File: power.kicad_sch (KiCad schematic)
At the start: 37 parts, among them J1 +5V SUPPLY, SW1 RESET, U1 NS32201, U19 74AHC32, U2 LM3671, U3 NS32016, U4 NS32082, U5 NS32202, U6 74AHC08, Y1 12.00000MHz

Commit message: merge in rev4
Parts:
- C7: value 2.2µF -> 0.1µF; footprint Capacitor_SMD:C_0603_1608Metric -> Capacitor_SMD:C_0402_1005Metric
- R6: value 47k -> 1k
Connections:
- net ~{RESET}: now also C7.1, R6.2, SW1.1, U1.7 (~{RSTI}); no longer U3.34 (~{RST}/ABT), U4.34 (~{RST}/ABT), U5.27 (~{RST})
- new net: U3.34 (~{RST}/ABT), U4.34 (~{RST}/ABT), U5.27 (~{RST})
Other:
- moved on the sheet: C1, C10, C11, C12, C14, C15, C16, C18, C2, C20, C3, C4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

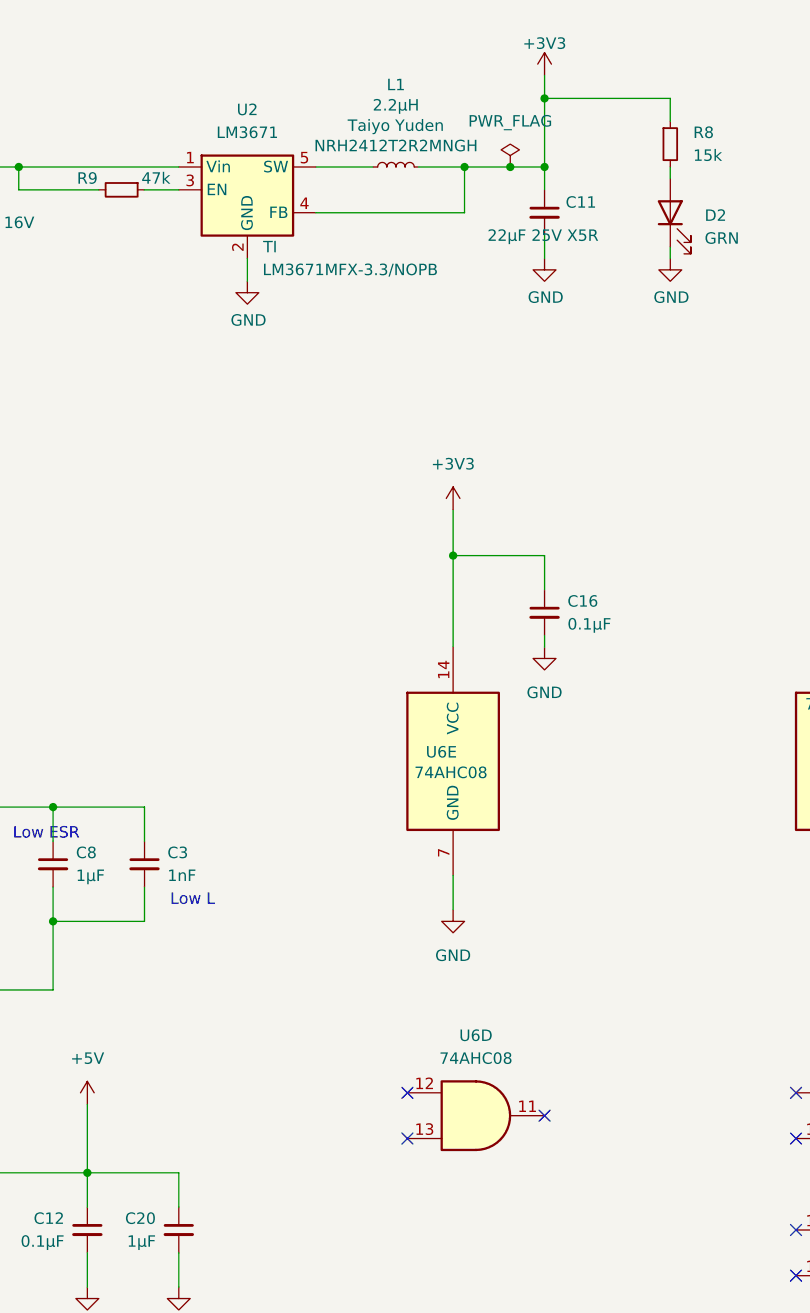
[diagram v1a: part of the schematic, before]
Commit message: fix address decoding
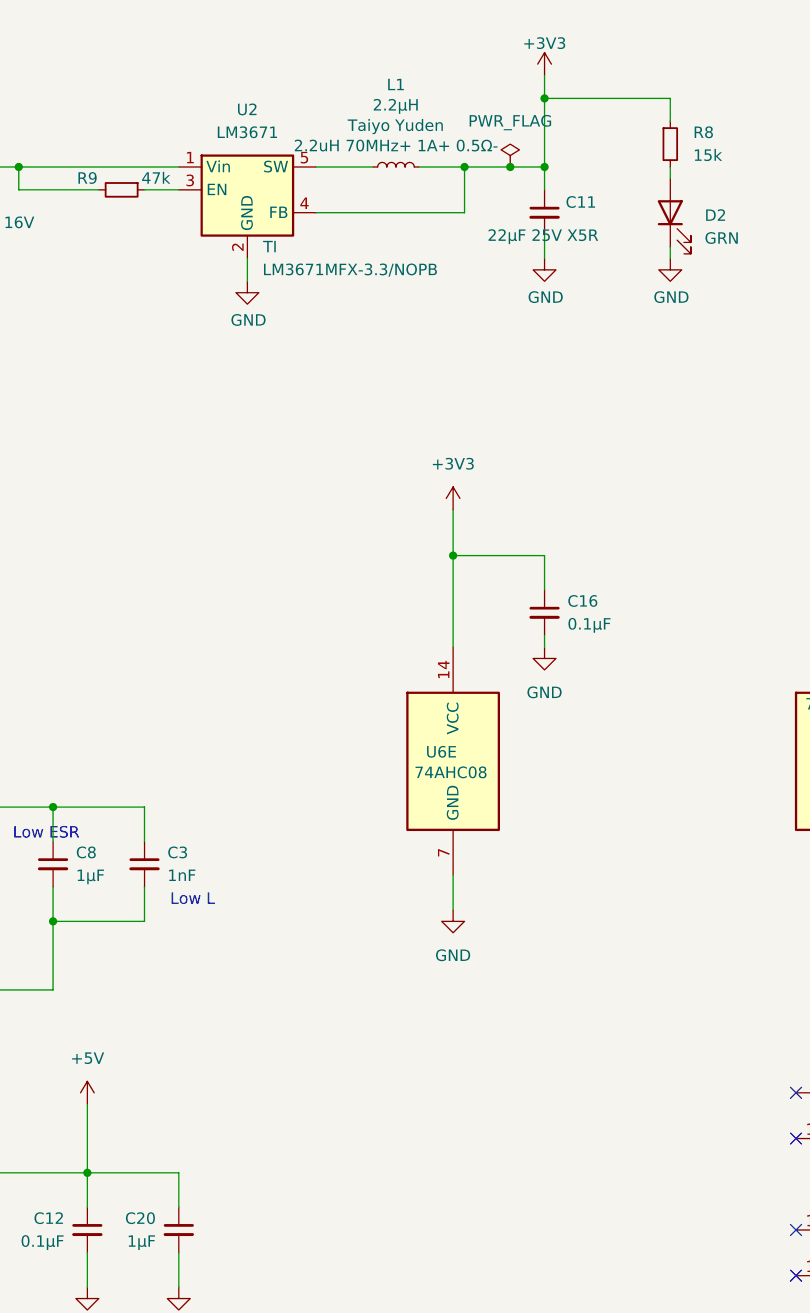
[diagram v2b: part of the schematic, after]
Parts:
- removed unit 4 of U6
- C1: LCSC (none) -> C312063
- C10, C14, C20, C5, C8: LCSC (none) -> C5189821
- C11: LCSC (none) -> C1864452
- C12, C15, C16, C18, C57, C6, C7: LCSC (none) -> C466613
- C2, C4: LCSC (none) -> C696895
- C3: LCSC (none) -> C189467
- C59: LCSC (none) -> C342606
- C9: LCSC (none) -> C3847478
- D1, D2: LCSC (none) -> C5246833
- L1: footprint Inductor_SMD:L_Taiyo-Yuden_NR-24xx -> Inductor_SMD:L_0805_2012Metric; LCSC (none) -> C6364734; Part NRH2412T2R2MNGH -> 2.2uH 70MHz+ 1A+ 0.5Ω-
- R1: LCSC (none) -> C186314
- R10: LCSC (none) -> C2906928
- R6: LCSC (none) -> C139047
- R8: LCSC (none) -> C478865
- R9: LCSC (none) -> C3017507
- U19: LCSC (none) -> C2868909
- U2: LCSC (none) -> C201586
- U6: LCSC (none) -> C2863502
- Y1: footprint FH12000001:FH12000001 -> Crystal:Crystal_SMD_3225-4Pin_3.2x2.5mm; LCSC (none) -> C7294547
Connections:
- no-connect marks 10 -> 7

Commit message: add rev4 gerbers, bom files
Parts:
- C11: value 22µF 25V X5R -> 22µF 25V
- J1: value +5V SUPPLY -> +5V SUPPLY DNP
- L1: value 2.2µH -> 2.2uH 70MHz+ 1A+ 0.5Ω-; Part 2.2uH 70MHz+ 1A+ 0.5Ω- -> (none)
- U2: value LM3671 -> LM3671 3.3V
- U3: value NS32016 -> NS32016 DNP
- U4: value NS32082 -> NS32082 DNP
- U5: value NS32202 -> NS32202 DNP
- Y1: Part FH1200001 -> (none)
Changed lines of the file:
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@@
 			)
 		)
-		(property "Value" "NS32202"
+		(property "Value" "NS32202 DNP"
 			(at 133.096 199.898 0)
 			(effects
@@
 			)
 		)
-		(property "Value" "NS32016"
+		(property "Value" "NS32016 DNP"
 			(at 200.914 124.714 0)
 			(effects
@@
 			)
 		)
-		(property "Value" "LM3671"
+		(property "Value" "LM3671 3.3V"
 			(at 242.57 48.26 0)
 			(effects
@@
 			)
 		)
-		(property "Value" "NS32082"
+		(property "Value" "NS32082 DNP"
 			(at 201.168 198.628 0)
 			(effects
@@
 			)
 		)
-		(property "Value" "2.2µH"
+		(property "Value" "2.2uH 70MHz+ 1A+ 0.5Ω-"
 			(at 259.08 45.212 90)
 			(effects
@@
 			)
 		)
-		(property "Part" "2.2uH 70MHz+ 1A+ 0.5Ω-"
+		(property "Part" ""
 			(at 259.08 49.7332 90)
 			(effects
@@
 			)
 		)
-		(property "Value" "+5V SUPPLY"
+		(property "Value" "+5V SUPPLY DNP"
 			(at 117.475 49.53 0)
 			(effects
@@
 			)
 		)
-		(property "Part" "FH1200001"
+		(property "Part" ""
 			(at 142.24 99.06 0)
 			(effects
@@
 			)
 		)
-		(property "Value" "22µF 25V X5R"
+		(property "Value" "22µF 25V"
 			(at 269.24 59.69 0)
 			(effects

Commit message: various changes, add LCSC part #s
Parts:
- C11: LCSC C1864452 -> C258782
- C12, C15, C16, C18, C57, C6, C7: LCSC C466613 -> C3012376
- C3: LCSC C189467 -> C696895
- C9: LCSC C3847478 -> C109457
- J1: value +5V SUPPLY DNP -> +5V SUPPLY
- R8: LCSC C478865 -> C850820
- U3: value NS32016 DNP -> NS32016
- U4: value NS32082 DNP -> NS32082
- U5: value NS32202 DNP -> NS32202
- U6: LCSC C2863502 -> C842279
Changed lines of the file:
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@@
 			)
 		)
-		(property "LCSC" "C2863502"
+		(property "LCSC" "C842279"
 			(at 265.43 118.11 0)
 			(effects
@@
 			)
 		)
-		(property "LCSC" "C466613"
+		(property "LCSC" "C3012376"
 			(at 224.79 170.18 0)
 			(effects
@@
 			)
 		)
-		(property "LCSC" "C466613"
+		(property "LCSC" "C3012376"
 			(at 91.44 109.22 0)
 			(effects
@@
 			)
 		)
-		(property "Value" "NS32202 DNP"
+		(property "Value" "NS32202"
 			(at 133.096 199.898 0)
 			(effects
@@
 			)
 		)
-		(property "LCSC" "C478865"
+		(property "LCSC" "C850820"
 			(at 289.56 49.53 0)
 			(effects
@@
 			)
 		)
-		(property "Value" "NS32016 DNP"
+		(property "Value" "NS32016"
 			(at 200.914 124.714 0)
 			(effects
@@
 			)
 		)
-		(property "LCSC" "C3847478"
+		(property "LCSC" "C109457"
 			(at 208.28 57.15 0)
 			(effects
@@
 			)
 		)
-		(property "LCSC" "C466613"
+		(property "LCSC" "C3012376"
 			(at 184.15 97.79 0)
 			(effects
@@
 			)
 		)
-		(property "LCSC" "C466613"
+		(property "LCSC" "C3012376"
 			(at 275.59 101.6 0)
 			(effects
@@
 			)
 		)
-		(property "LCSC" "C466613"
+		(property "LCSC" "C3012376"
 			(at 85.09 147.32 0)
 			(effects
@@
 			)
 		)
-		(property "Value" "NS32082 DNP"
+		(property "Value" "NS32082"
 			(at 201.168 198.628 0)
 			(effects
@@
 			)
 		)
-		(property "Value" "+5V SUPPLY DNP"
+		(property "Value" "+5V SUPPLY"
 			(at 117.475 49.53 0)
 			(effects
@@
 			)
 		)
-		(property "LCSC" "C466613"
+		(property "LCSC" "C3012376"
 			(at 110.49 179.07 0)
 			(effects
@@
 			)
 		)
-		(property "LCSC" "C189467"
+		(property "LCSC" "C696895"
 			(at 231.14 129.54 0)
 			(effects
@@
 			)
 		)
-		(property "LCSC" "C1864452"
+		(property "LCSC" "C258782"
 			(at 275.59 57.15 0)
 			(effects
@@
 			)
 		)
-		(property "LCSC" "C466613"
+		(property "LCSC" "C3012376"
 			(at 318.77 101.6 0)
 			(effects

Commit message: revert crystal footprints back from LCSC parts
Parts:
- Y1: footprint Crystal:Crystal_SMD_3225-4Pin_3.2x2.5mm -> FH12000001:FH12000001
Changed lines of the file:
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@@
 			)
 		)
-		(property "Footprint" "Crystal:Crystal_SMD_3225-4Pin_3.2x2.5mm"
+		(property "Footprint" "FH12000001:FH12000001"
 			(at 127 100.33 0)
 			(effects

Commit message: cleanups
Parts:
- L1: value 2.2uH 70MHz+ 1A+ 0.5Ω- -> 2.2µH 70MHz+ 1A+ 0.5Ω-; Mfg Taiyo Yuden -> (none)
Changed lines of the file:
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@@
 		(dnp no)
 		(property "Reference" "L1"
-			(at 259.08 42.9514 90)
+			(at 262.89 51.308 90)
 			(effects
 				(font
@@
 			)
 		)
-		(property "Value" "2.2uH 70MHz+ 1A+ 0.5Ω-"
-			(at 259.08 45.212 90)
+		(property "Value" "2.2µH 70MHz+ 1A+ 0.5Ω-"
+			(at 262.89 53.5686 90)
 			(effects
 				(font
@@
 			)
 		)
-		(property "Mfg" "Taiyo Yuden"
-			(at 259.08 47.4726 90)
-			(effects
-				(font
-					(size 1.27 1.27)
-				)
-			)
-		)
-		(property "Part" ""
-			(at 259.08 49.7332 90)
-			(effects
-				(font
-					(size 1.27 1.27)
-				)
-			)
-		)

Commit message: restore L1 TY NHR24xx FP
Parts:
- L1: footprint Inductor_SMD:L_0805_2012Metric -> Inductor_SMD:L_Taiyo-Yuden_NR-24xx
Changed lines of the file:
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@@
 			)
 		)
-		(property "Footprint" "Inductor_SMD:L_0805_2012Metric"
+		(property "Footprint" "Inductor_SMD:L_Taiyo-Yuden_NR-24xx"
 			(at 259.08 52.07 0)
 			(effects

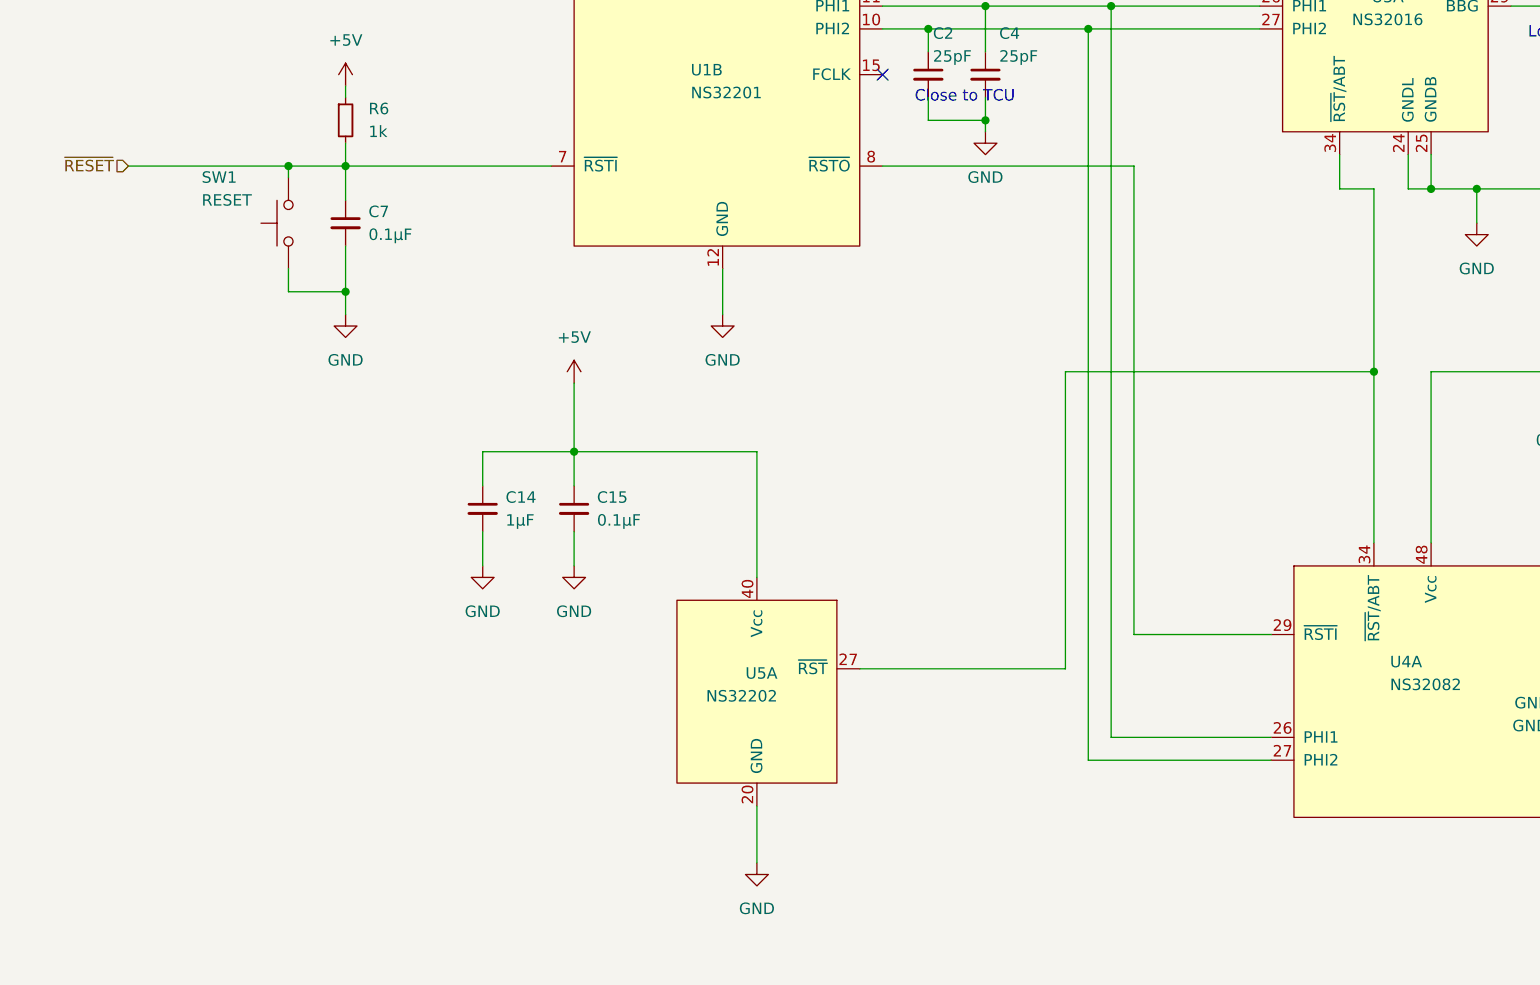
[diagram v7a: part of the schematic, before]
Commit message: rev4 errata, fix in main
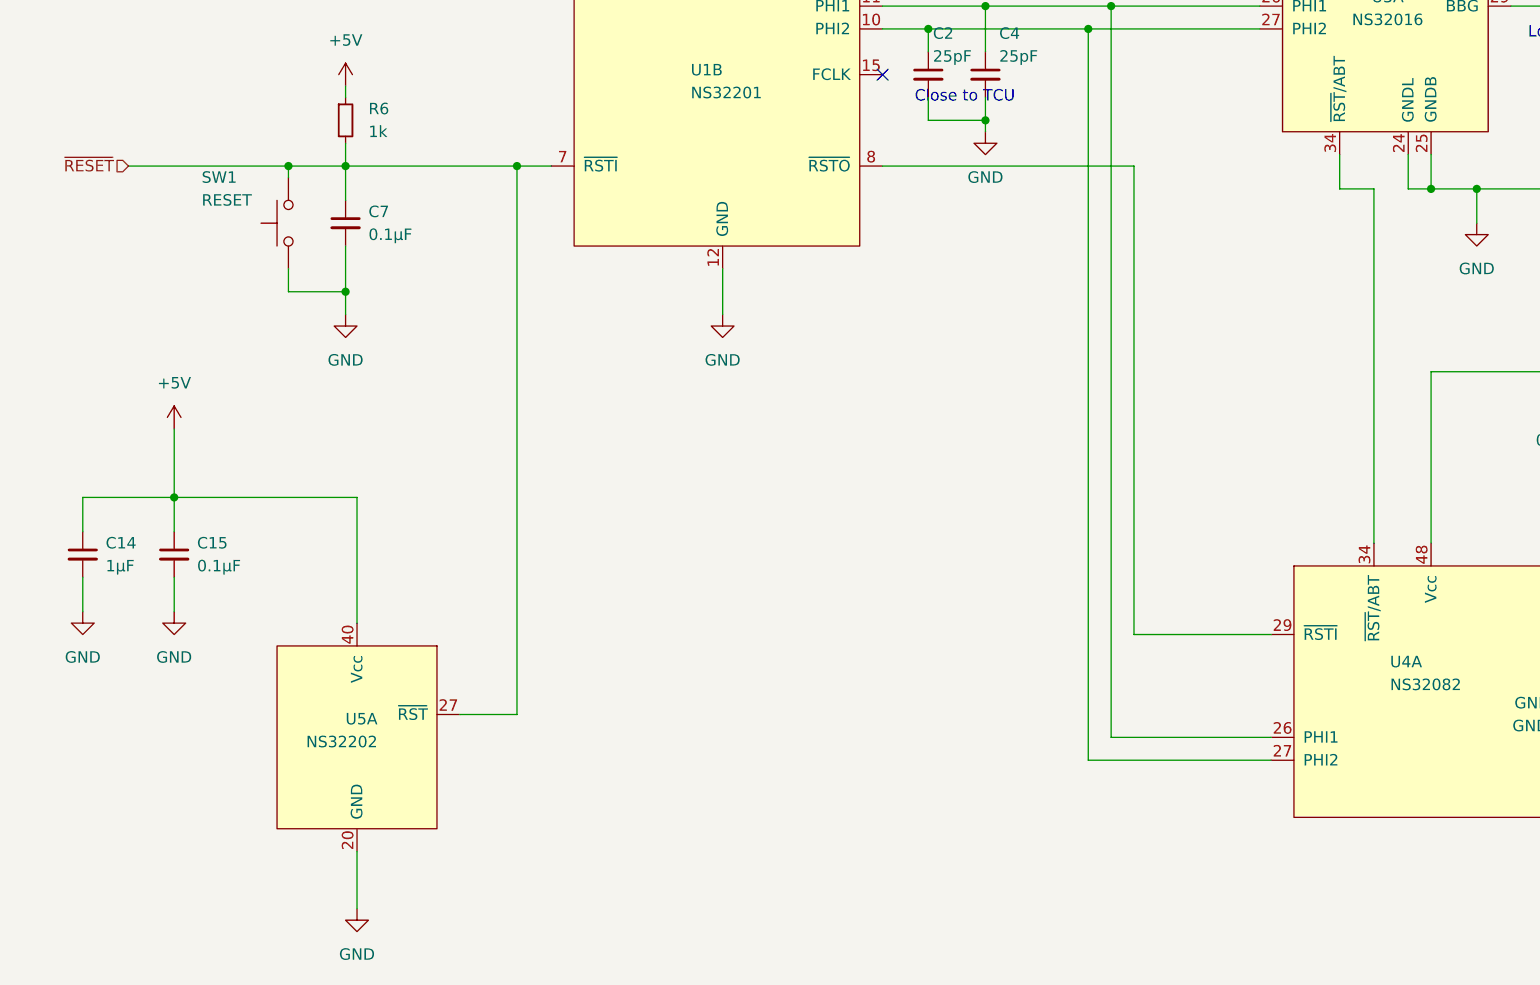
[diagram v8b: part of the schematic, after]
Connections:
- net ~{RESET}: now also U5.27 (~{RST})
- net at U3.34 (~{RST}/ABT), U4.34 (~{RST}/ABT): no longer U5.27 (~{RST})
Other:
- moved on the sheet: C14, C15, U5A
